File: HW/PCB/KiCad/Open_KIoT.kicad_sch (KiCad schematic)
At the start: 52 parts, among them J1 Jack-DC, J2 Conn_01x03, J3 Conn_01x03, J4 Conn_01x03, J5 Conn_01x08, J6 Conn_01x08, J7 Conn_01x08, J8 Conn_01x11, SW1 SW_DIP_x01, SW2 SW_DIP_x01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

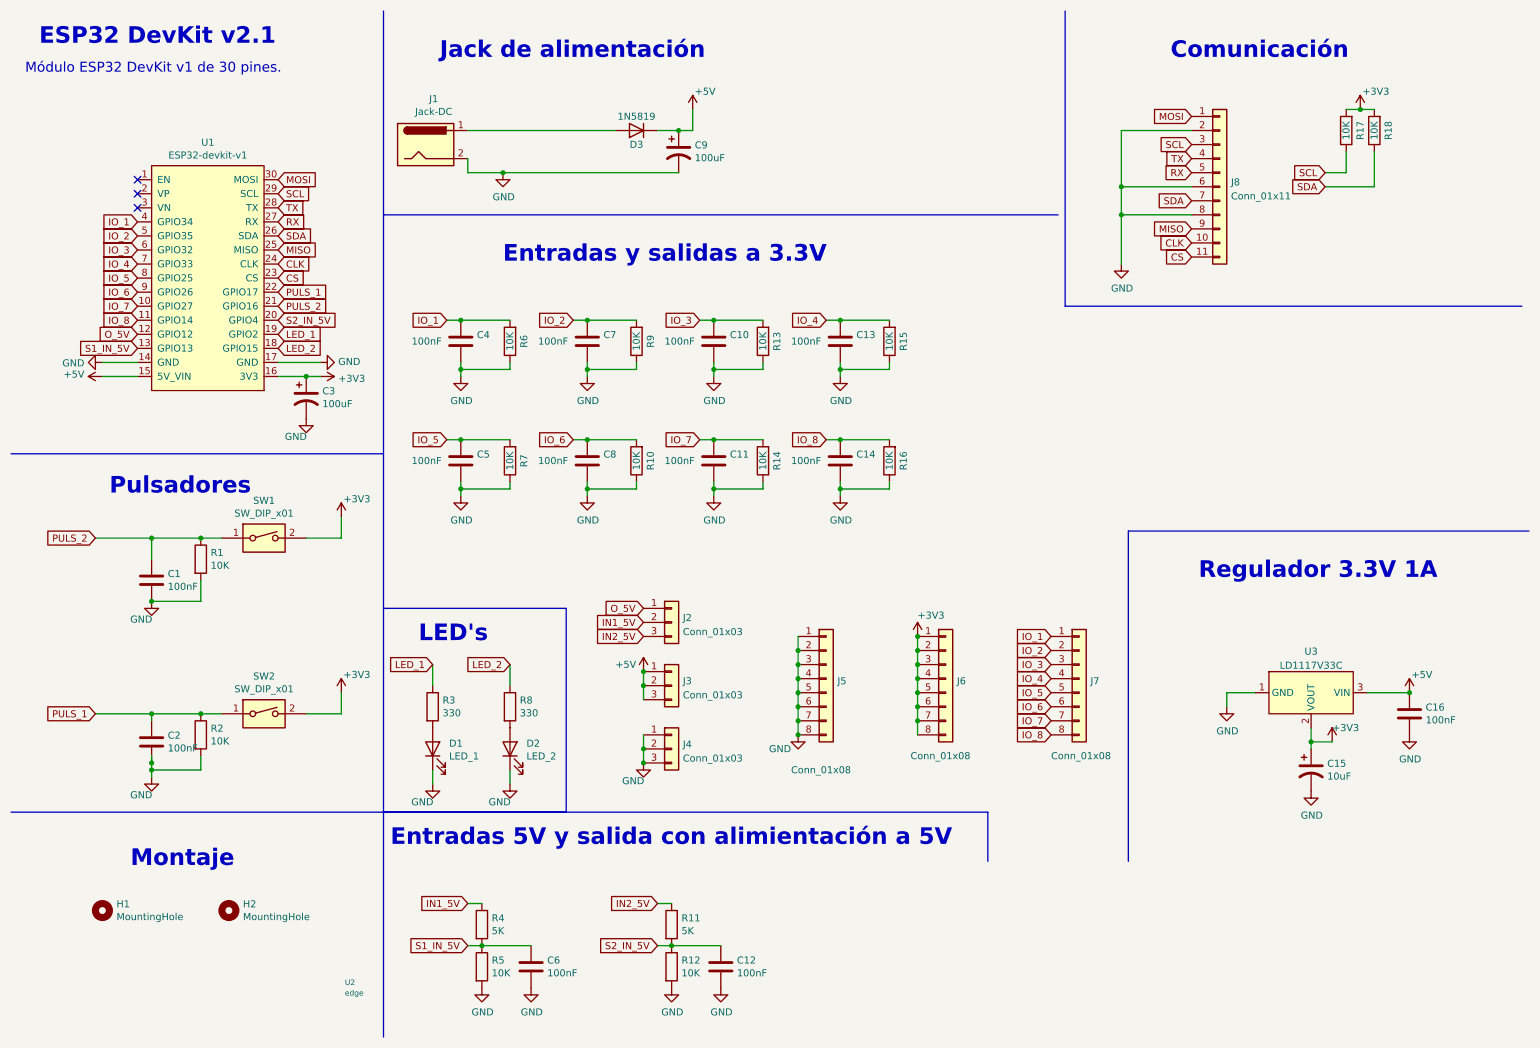
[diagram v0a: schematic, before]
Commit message: Corrección errores valores resistencias
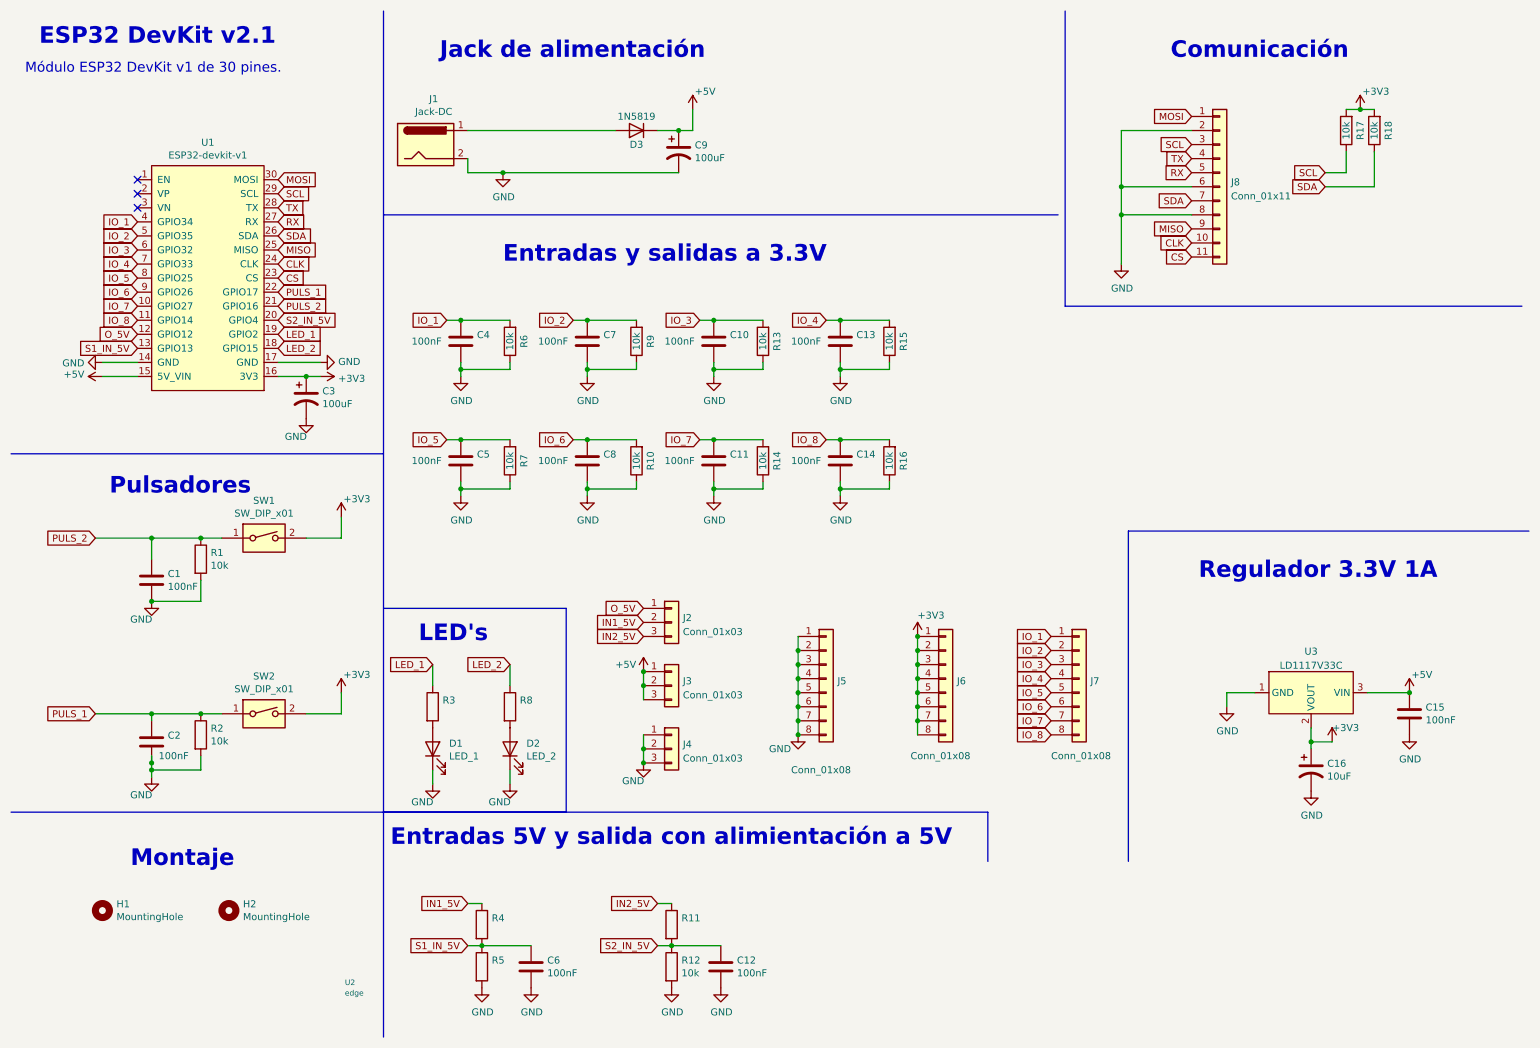
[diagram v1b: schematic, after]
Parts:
- R1, R10, R12, R13, R14, R15, R16, R17, R18, R2, R6, R7, R9: value 10K -> 10k
- R11, R4: value 5K -> (none)
- R3, R8: value 330 -> (none)
- R5: value 10K -> (none)
- renumbered C16 to C15, C15 to C16

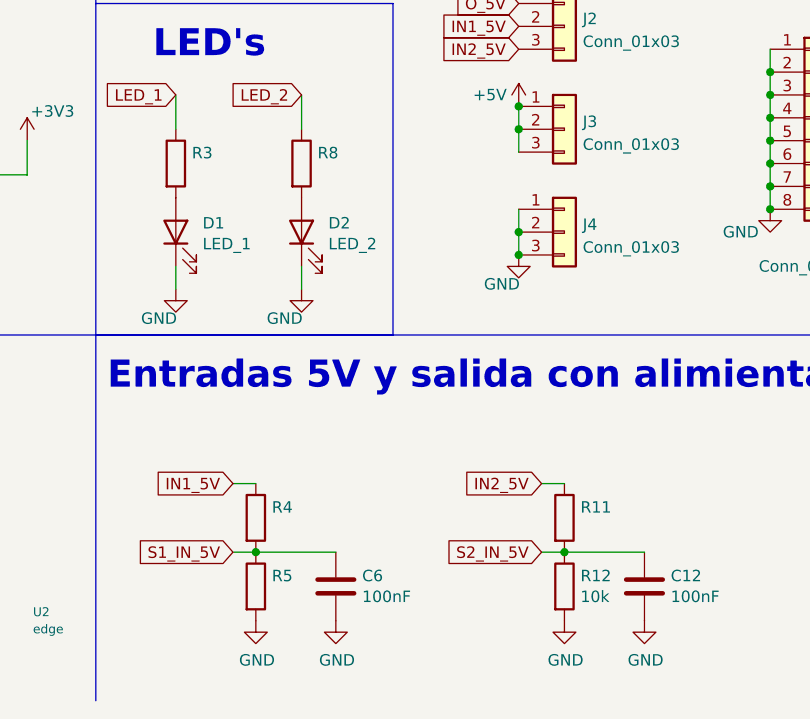
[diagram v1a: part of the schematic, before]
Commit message: Corrección error esquema
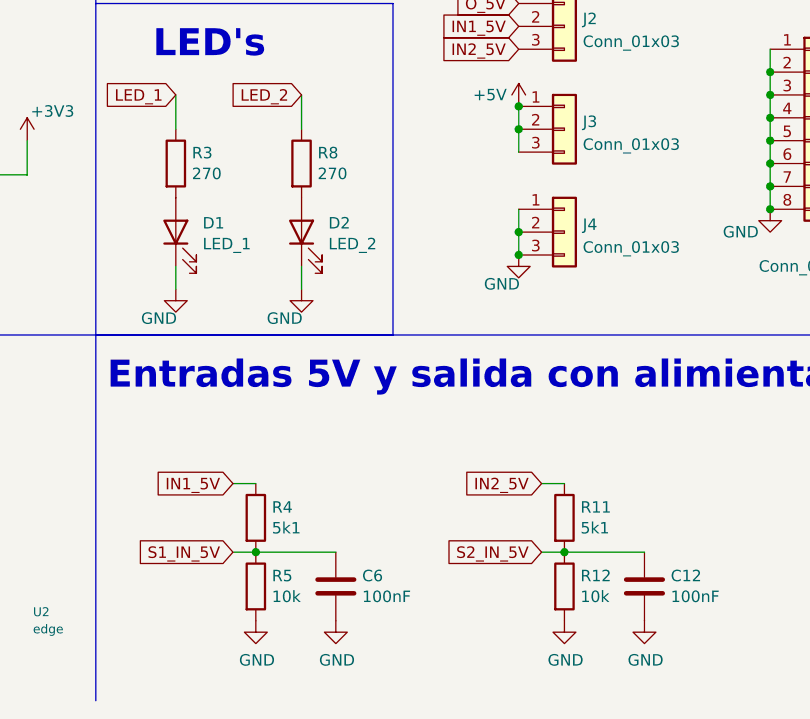
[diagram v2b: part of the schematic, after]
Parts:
- R11, R4: value (none) -> 5k1
- R3, R8: value (none) -> 270
- R5: value (none) -> 10k
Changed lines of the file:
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@@
       (effects (font (size 1.27 1.27)) (justify left))
     )
-    (property "Value" "" (id 1) (at 89.408 139.573 0)
+    (property "Value" "270" (id 1) (at 89.408 139.573 0)
       (effects (font (size 1.27 1.27)) (justify left))
     )
@@
       (effects (font (size 1.27 1.27)) (justify left))
     )
-    (property "Value" "" (id 1) (at 103.378 139.573 0)
+    (property "Value" "270" (id 1) (at 103.378 139.573 0)
       (effects (font (size 1.27 1.27)) (justify left))
     )
@@
       (effects (font (size 1.27 1.27)) (justify left))
     )
-    (property "Value" "" (id 1) (at 98.298 178.943 0)
+    (property "Value" "5k1" (id 1) (at 98.298 178.943 0)
       (effects (font (size 1.27 1.27)) (justify left))
     )
@@
       (effects (font (size 1.27 1.27)) (justify left))
     )
-    (property "Value" "" (id 1) (at 132.588 178.943 0)
+    (property "Value" "5k1" (id 1) (at 132.588 178.943 0)
       (effects (font (size 1.27 1.27)) (justify left))
     )
@@
       (effects (font (size 1.27 1.27)) (justify left))
     )
-    (property "Value" "" (id 1) (at 98.298 186.563 0)
-      (effects (font (size 1.27 1.27)) (justify left))
-    )
+    (property "Value" "10k" (id 1) (at 98.298 186.563 0)
+      (effects (font (size 1.27 1.27)) (justify left))
+    )
